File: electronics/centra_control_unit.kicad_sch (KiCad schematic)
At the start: 38 parts, among them J1 GND NetTie, J2 CAN Conn, J3 Conn 12V Out 5ch, J4 Conn_01x02, U1 AZ1117-ADJ, U10 BTS7006, U2 AZ1117-ADJ, U3 TJA1051T-3, U4 ESP32-S3-MINI-1U, U5 CD74HC4067SM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

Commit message: from Legion
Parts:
- removed J4: Conn_01x02, TerminalBlock_MetzConnect:TerminalBlock_MetzConnect_Type703_RT10N02HGLU_1x02_P9.52mm_Horizontal, symbol Connector_Generic:Conn_01x02
- added J10: water_sensor_conn, TerminalBlock:TerminalBlock_Xinya_XY308-2.54-6P_1x06_P2.54mm_Horizontal, symbol Connector_Generic:Conn_01x06
- added Q2, Q3: IRF6802SD, Package_DirectFET:DirectFET_SA, symbol Transistor_FET:IRF6802SD
- J2: value CAN Conn -> CAN
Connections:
- net V_Bat is gone; now on net +BATT: D1.2 (A), U10.15 (VS), U6.15 (VS), U7.15 (VS), U8.15 (VS), U9.15 (VS)
- net CAN_H: now also J2.1 (Pin_1); no longer J2.2 (Pin_2)
- net CAN_L: now also J2.2 (Pin_2); no longer J2.1 (Pin_1)
- net CAN_RX: now also U4.13 (IO9); no longer U4.15 (IO11)
- net CAN_SLEEP: now also U4.14 (IO10); no longer U4.16 (IO12)
- net CAN_TX: now also U4.12 (IO8); no longer U4.14 (IO10)
- net CH1_DIAG_EN: now also U4.27 (IO47)
- net CH2_DAIG_EN: now also U4.37 (IO41)
- net CH2_IN: now also U4.38 (IO42)
- net CH3_DAIG_EN: now also U4.35 (IO39)
- net CH3_IN: now also U4.36 (IO40)
- net CH4_DAIG_EN: now also U4.33 (IO37)
- net CH4_DIAG: no longer U10.4 (IS)
- net CH4_IN: now also U4.34 (IO38)
- net CH5_DAIG_EN: now also U4.31 (IO35)
- net CH5_DIAG: now also U10.4 (IS)
- net CH5_IN: now also U4.32 (IO36)
- net GND: no longer C3.1, R4.2
- net MUX_ANALOG_COM: now also U4.16 (IO12)
- net MUX_S0: now reaches U5.10 (S0)
- net MUX_S0: now also U4.20 (IO16)
- net MUX_S1: now reaches U5.11 (S1)
- net MUX_S1: now also U4.19 (IO15)
- net MUX_S3: now reaches U5.13 (S3)
- net MUX_S3: now also U4.17 (IO13)
- net MUX_S2: now reaches U5.14 (S2)
- net MUX_S2: now also U4.18 (IO14)
- net ws_lvl_5: now reaches U5.16 (I15)
- net ws_lvl_5: now also J10.6 (Pin_6)
- net ws_lvl_4: now reaches U5.17 (I14)
- net ws_lvl_4: now also J10.5 (Pin_5)
- net ws_lvl_3: now reaches U5.18 (I13)
- net ws_lvl_3: now also J10.4 (Pin_4)
- net ws_lvl_2: now reaches U5.19 (I12)
- net ws_lvl_2: now also J10.3 (Pin_3)
- net ws_lvl_1: now reaches U5.20 (I11)
- net ws_lvl_1: now also J10.2 (Pin_2)
- net SDA: now reaches U4.10 (IO6)
- net SCL: now reaches U4.11 (IO7)
- net LED_B: now reaches U4.26 (IO26)
- net LED_G: now reaches U4.28 (IO33)
- net LED_R: now reaches U4.29 (IO34)
- net +12V renamed 12V_MCU
- net +3V3: no longer names the net of U3.5 (VIO)
- new net water_sens_enable: J10.1 (Pin_1), U4.15 (IO11)
- no-connect marks 36 -> 19
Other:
- note added: "LED controls"
- moved on the sheet: J1, J2, U3

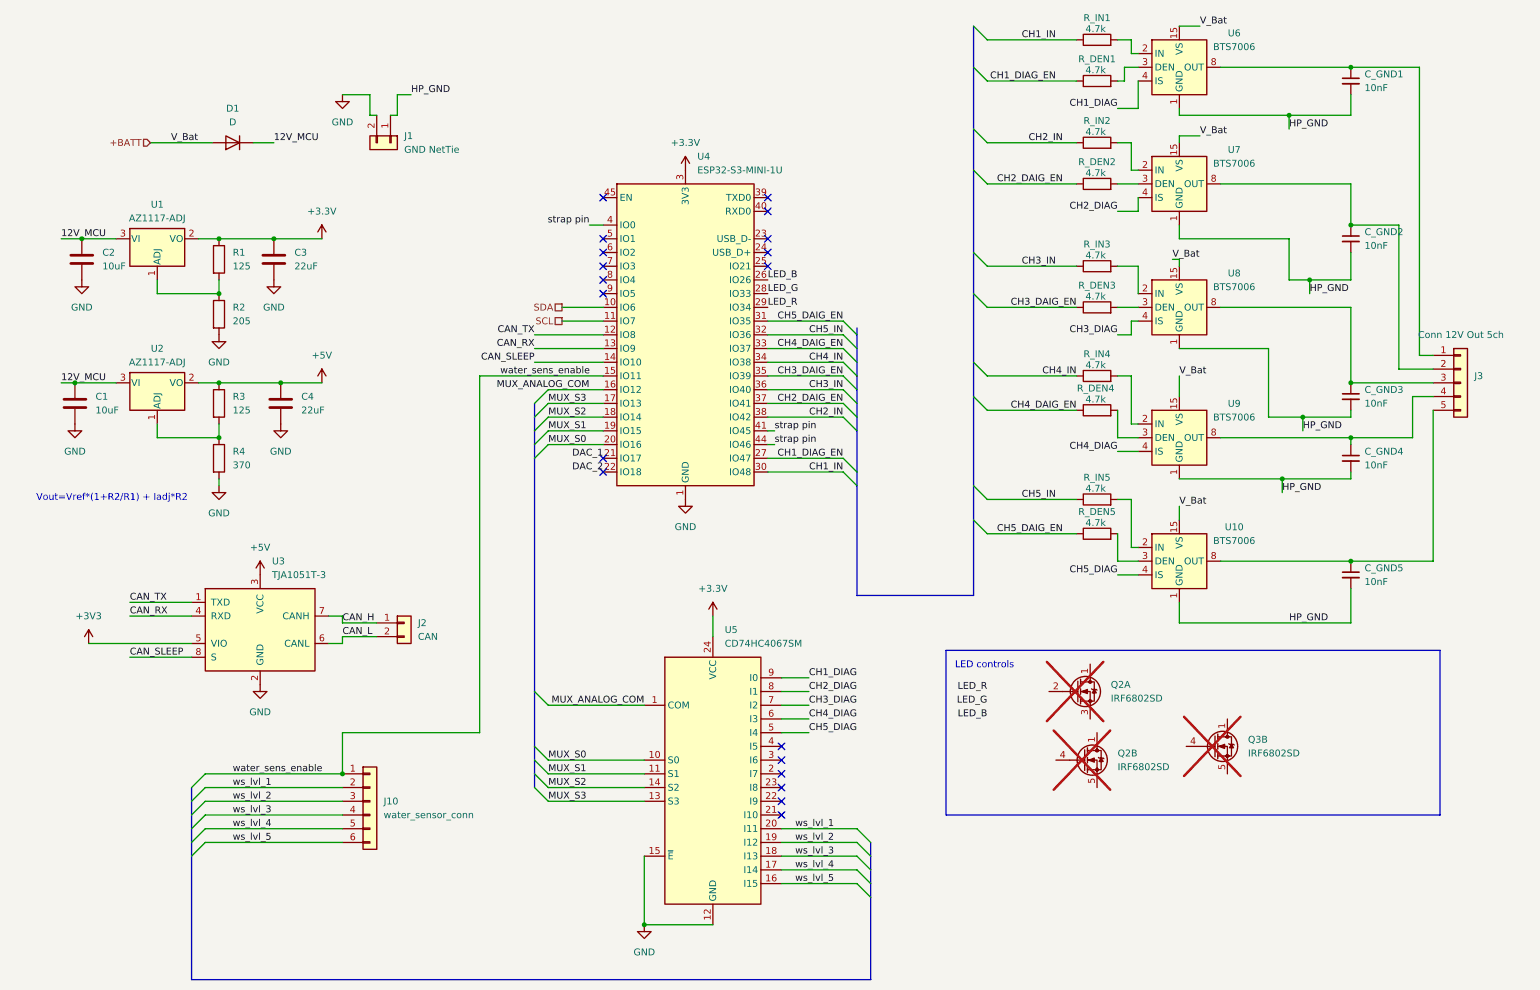
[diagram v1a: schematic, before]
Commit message: big-55A-switch added
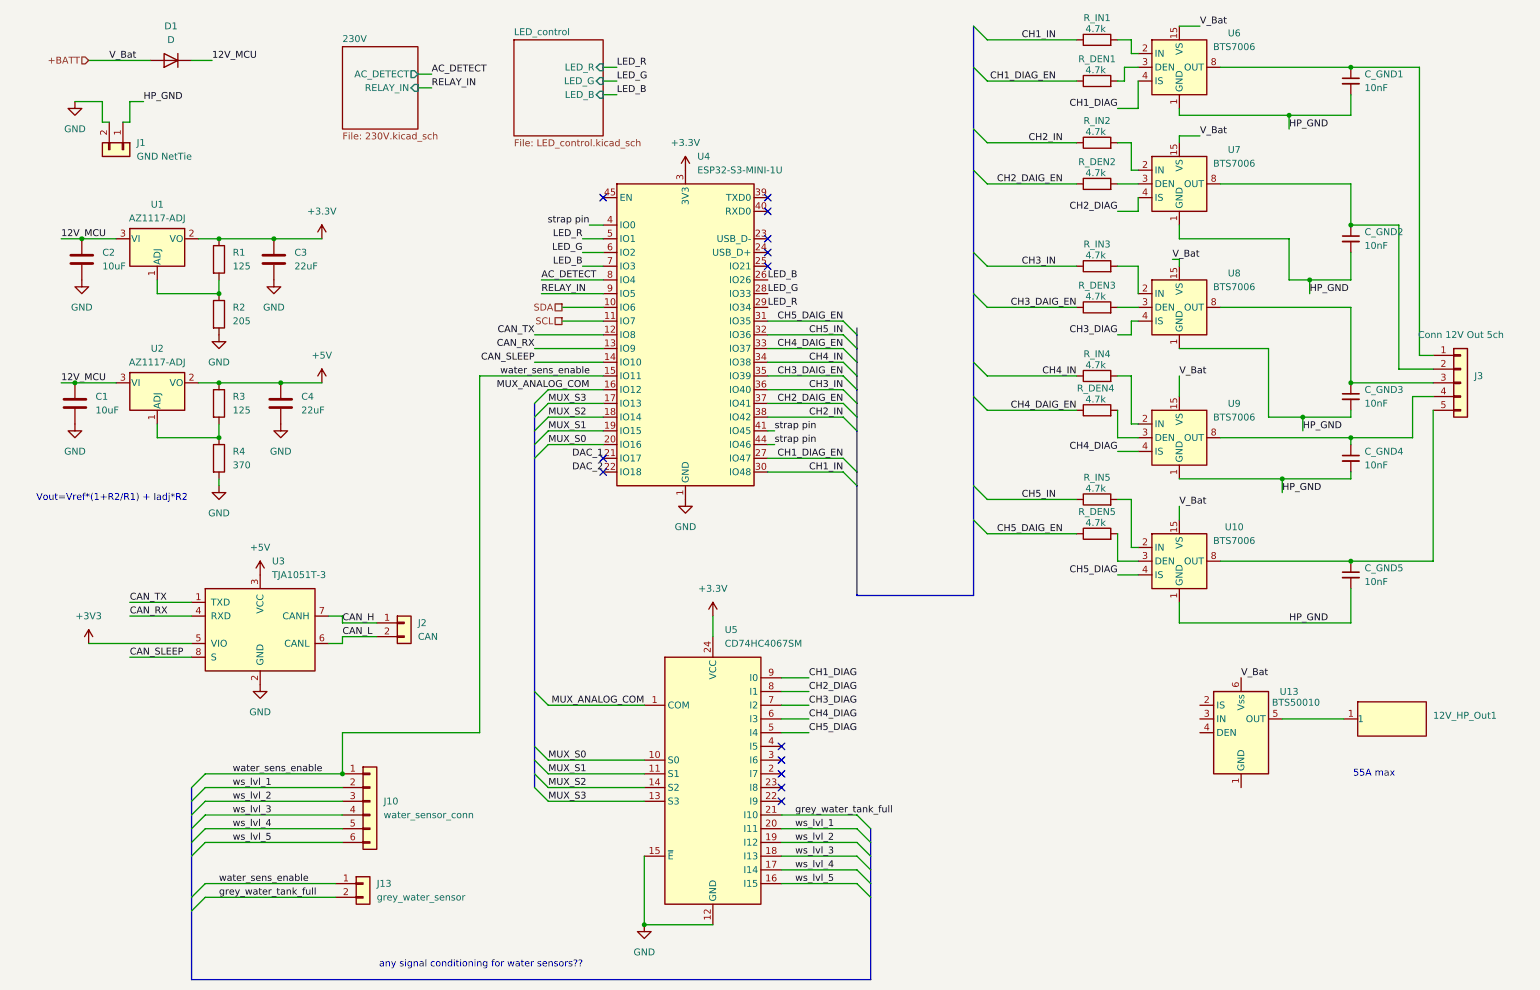
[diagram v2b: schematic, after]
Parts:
- removed Q2, Q3: IRF6802SD, Package_DirectFET:DirectFET_SA, symbol Transistor_FET:IRF6802SD
- added 12V_HP_Out1: ~, HeavyDuty:high_current_pad, symbol HeavyDuty:BusBarConn
- added J13: grey_water_sensor, TerminalBlock:TerminalBlock_Xinya_XY308-2.54-2P_1x02_P2.54mm_Horizontal, symbol Connector_Generic:Conn_01x02
- added U13: BTS50010, HeavyDuty:PG-HSOF-8, symbol HeavyDuty:BTS50010
- U4: footprint RF_Module:ESP32-S2-MINI-1U -> PCM_Espressif:ESP32-S2-MINI-1U
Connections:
- net +BATT: now also U13.6 (Vss)
- net LED_B: now also U4.7 (IO3)
- net LED_G: now also U4.6 (IO2)
- net LED_R: now also U4.5 (IO1)
- net water_sens_enable: now also J13.1 (Pin_1)
- net grey_water_tank_full: now reaches U5.21 (I10)
- net grey_water_tank_full: now also J13.2 (Pin_2)
- net AC_DETECT: now reaches U4.8 (IO4)
- net RELAY_IN: now reaches U4.9 (IO5)
- new net: 12V_HP_Out1.1, U13.5 (OUT), U13.6 (Vss), U13.7 (OUT)
- no-connect marks 19 -> 13
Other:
- added sheet 230V (230V.kicad_sch)
- added sheet LED_control (LED_control.kicad_sch)
- note added: "55A max"
- note added: "any signal conditioning for water sensors??"
- note removed: "LED controls"
- moved on the sheet: D1, J1

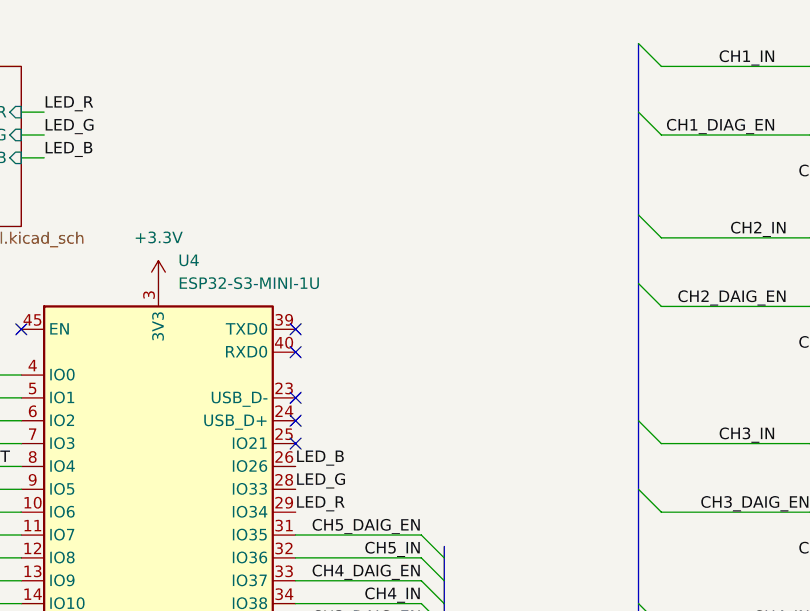
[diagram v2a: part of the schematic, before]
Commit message: LED RGB and temp sensor added
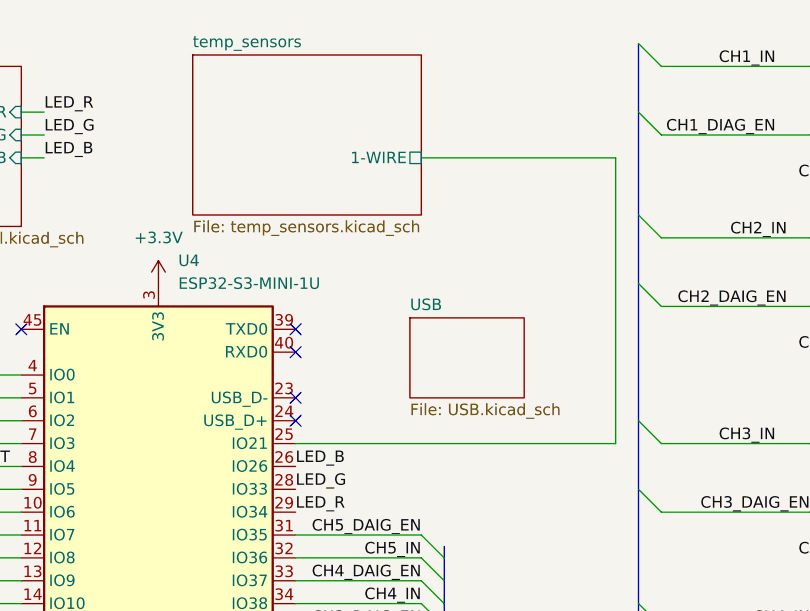
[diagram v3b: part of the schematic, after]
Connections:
- net temp_sensors/1-WIRE: now reaches U4.25 (IO21)
- no-connect marks 13 -> 12
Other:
- added sheet USB (USB.kicad_sch)
- added sheet temp_sensors (temp_sensors.kicad_sch)
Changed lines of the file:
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@@
 	)
 	(no_connect
-		(at 146.05 60.96)
-	)
-	(no_connect
 		(at 115.57 48.26)
 	)
@@
 	(wire
 		(pts
+			(xy 160.02 29.21) (xy 181.61 29.21)
+		)
+		(stroke
+			(width 0)
+			(type default)
+		)
+	)
+	(wire
+		(pts
 			(xy 41.91 160.02) (xy 67.31 160.02)
 		)
@@
 		)
 	)
+	(wire
+		(pts
+			(xy 181.61 29.21) (xy 181.61 60.96)
+		)
+		(stroke
+			(width 0)
+			(type default)
+		)
+	)
 	(bus
 		(pts
@@
 	(wire
 		(pts
+			(xy 181.61 60.96) (xy 146.05 60.96)
+		)
+		(stroke
+			(width 0)
+			(type default)
+		)
+	)
+	(wire
+		(pts
 			(xy 222.25 60.96) (xy 222.25 59.69)
 		)
@@
 				)
 			)
+		)
+	)
+	(sheet
+		(at 134.62 17.78)
+		(size 25.4 17.78)
+		(fields_autoplaced yes)
+		(stroke
+			(width 0.1524)
+			(type solid)
+		)
+		(fill
+			(color 0 0 0 0.0000)
+		)
+		(property "Sheetname" "temp_sensors"
+			(at 134.62 17.0684 0)
+			(effects
+				(font
+					(size 1.27 1.27)
+				)
+				(justify left bottom)
+			)
+		)
+		(property "Sheetfile" "temp_sensors.kicad_sch"
+			(at 134.62 36.1446 0)
+			(effects
+				(font
+					(size 1.27 1.27)
+				)
+				(justify left top)
+			)
+		)
+		(pin "1-WIRE" passive
+			(at 160.02 29.21 0)
+			(effects
+				(font
+					(size 1.27 1.27)
+				)
+				(justify right)
+			)
+		)
+		(instances
+			(project "electronics"
+				(path "/eeb1234c-eae0-4ac6-a30d-2a978d66d889/04c402f1-b99a-4823-99a0-0c7312782f29"
+					(page "8")
+				)
+			)
+		)
+	)
+	(sheet
+		(at 158.75 46.99)
+		(size 12.7 8.89)
+		(fields_autoplaced yes)
+		(stroke
+			(width 0.1524)
+			(type solid)
+		)
+		(fill
+			(color 0 0 0 0.0000)
+		)
+		(property "Sheetname" "USB"
+			(at 158.75 46.2784 0)
+			(effects
+				(font
+					(size 1.27 1.27)
+				)
+				(justify left bottom)
+			)
+		)
+		(property "Sheetfile" "USB.kicad_sch"
+			(at 158.75 56.4646 0)
+			(effects
+				(font
+					(size 1.27 1.27)
+				)
+				(justify left top)
+			)
+		)
+		(instances
+			(project "electronics"
+				(path "/eeb1234c-eae0-4ac6-a30d-2a978d66d889/04c402f1-b99a-4823-99a0-0c7312782f29"
+					(page "9")
+				)
+			)
